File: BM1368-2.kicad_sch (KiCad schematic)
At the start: 39 parts, among them U12 BM1368_mode1, U13 BM1368_mode1

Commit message: DRC Check
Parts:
- removed R51: 10k, Resistor_SMD:R_0805_2012Metric, symbol Device:R
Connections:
- net U13-VDD1_1: now reaches C146.2, C147.1, U13.28 (VDD1_1)
- net U13-VDD2_1: now reaches C145.2, C146.1, U13.29 (VDD2_1)
- net U13-VDD3_1: now reaches C144.2, C145.1, U13.30 (VDD3_1)
- net Net-(U11-VDD1_1) renamed U11-VDD1_1
- net Net-(U11-VDD2_1) renamed U11-VDD2_1
- net Net-(U11-VDD3_1) renamed U11-VDD3_1
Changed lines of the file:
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@@
 	)
 	(junction
+		(at 234.95 45.72)
+		(diameter 0)
+		(color 0 0 0 0)
+	)
+	(junction
+		(at 257.81 50.8)
+		(diameter 0)
+		(color 0 0 0 0)
+	)
+	(junction
 		(at 184.15 36.83)
 		(diameter 0)
@@
 	)
 	(junction
+		(at 78.74 45.72)
+		(diameter 0)
+		(color 0 0 0 0)
+	)
+	(junction
+		(at 54.61 50.8)
+		(diameter 0)
+		(color 0 0 0 0)
+	)
+	(junction
 		(at 139.7 55.88)
 		(diameter 0)
@@
 	)
 	(junction
+		(at 67.31 48.26)
+		(diameter 0)
+		(color 0 0 0 0)
+	)
+	(junction
 		(at 234.95 53.34)
 		(diameter 0)
@@
 	)
 	(junction
-		(at 234.95 76.2)
+		(at 246.38 48.26)
 		(diameter 0)
 		(color 0 0 0 0)
 	)
 	(junction
-		(at 97.79 36.83)
+		(at 234.95 76.2)
 		(diameter 0)
 		(color 0 0 0 0)
 	)
 	(junction
-		(at 254 55.88)
+		(at 97.79 36.83)
 		(diameter 0)
 		(color 0 0 0 0)
@@
 	(wire
 		(pts
+			(xy 257.81 50.8) (xy 275.59 50.8)
+		)
+		(stroke
+			(width 0)
+			(type default)
+		)
+	)
+	(wire
+		(pts
 			(xy 181.61 71.12) (xy 196.85 71.12)
 		)
@@
 	(wire
 		(pts
-			(xy 254 55.88) (xy 254 77.47)
-		)
-		(stroke
-			(width 0)
-			(type default)
-		)
-	)
-	(wire
-		(pts
 			(xy 97.79 34.29) (xy 97.79 36.83)
 		)
@@
 	(wire
 		(pts
-			(xy 254 55.88) (xy 274.32 55.88)
+			(xy 232.41 55.88) (xy 274.32 55.88)
 		)
 		(stroke
@@
 	(wire
 		(pts
+			(xy 30.48 45.72) (xy 78.74 45.72)
+		)
+		(stroke
+			(width 0)
+			(type default)
+		)
+	)
+	(wire
+		(pts
 			(xy 214.63 36.83) (xy 222.25 36.83)
 		)
@@
 	(wire
 		(pts
-			(xy 214.63 86.36) (xy 214.63 91.44)
+			(xy 246.38 48.26) (xy 275.59 48.26)
 		)
 		(stroke
@@
 	(wire
 		(pts
-			(xy 195.58 36.83) (xy 195.58 45.72)
+			(xy 214.63 86.36) (xy 214.63 91.44)
 		)
 		(stroke
@@
 	(wire
 		(pts
-			(xy 254 85.09) (xy 254 87.63)
+			(xy 195.58 36.83) (xy 195.58 45.72)
 		)
 		(stroke
@@
 	(wire
 		(pts
+			(xy 234.95 45.72) (xy 275.59 45.72)
+		)
+		(stroke
+			(width 0)
+			(type default)
+		)
+	)
+	(wire
+		(pts
 			(xy 73.66 146.05) (xy 73.66 147.32)
 		)
@@
 	(wire
 		(pts
-			(xy 257.81 50.8) (xy 257.81 36.83)
+			(xy 30.48 48.26) (xy 67.31 48.26)
 		)
 		(stroke
@@
 	(wire
 		(pts
-			(xy 232.41 55.88) (xy 254 55.88)
+			(xy 257.81 50.8) (xy 257.81 36.83)
 		)
 		(stroke
@@
 	(wire
 		(pts
+			(xy 30.48 50.8) (xy 54.61 50.8)
+		)
+		(stroke
+			(width 0)
+			(type default)
+		)
+	)
+	(wire
+		(pts
 			(xy 78.74 36.83) (xy 78.74 45.72)
 		)
@@
 		)
 	)
-	(label "Net-(U11-VDD3_1)"
-		(at 78.74 36.83 90)
+	(hierarchical_label "NRSTO"
+		(shape output)
+		(at 274.32 55.88 0)
 		(fields_autoplaced yes)
 		(effects
@@
 				(size 1.27 1.27)
 			)
-			(justify left bottom)
+			(justify left)
 		)
 	)
-	(label "Net-(U11-VDD1_1)"
-		(at 54.61 50.8 0)
+	(hierarchical_label "RI"
+		(shape input)
+		(at 270.51 60.96 0)
 		(fields_autoplaced yes)
 		(effects
@@
 				(size 1.27 1.27)
 			)
-			(justify left bottom)
+			(justify left)
 		)
 	)
-	(label "Net-(U11-VDD2_1)"
-		(at 67.31 36.83 90)
+	(hierarchical_label "U11-VDD3_1"
+		(shape input)
+		(at 30.48 45.72 180)
 		(fields_autoplaced yes)
 		(effects
@@
 				(size 1.27 1.27)
 			)
-			(justify left bottom)
+			(justify right)
 		)
 	)
-	(hierarchical_label "NRSTO"
+	(hierarchical_label "BI"
+		(shape input)
+		(at 62.23 66.04 180)
+		(fields_autoplaced yes)
+		(effects
+			(font
+				(size 1.27 1.27)
+			)
+			(justify right)
+		)
+	)
+	(hierarchical_label "U13-VDD2_1"
 		(shape output)
-		(at 274.32 55.88 0)
+		(at 275.59 48.26 0)
 		(fields_autoplaced yes)
 		(effects
@@
 		)
 	)
-	(hierarchical_label "RI"
-		(shape input)
-		(at 270.51 60.96 0)
+	(hierarchical_label "CLKO"
+		(shape output)
+		(at 269.24 63.5 0)
 		(fields_autoplaced yes)
 		(effects
@@
 		)
 	)
-	(hierarchical_label "BI"
+	(hierarchical_label "CI"
 		(shape input)
-		(at 62.23 66.04 180)
+		(at 60.96 58.42 180)
 		(fields_autoplaced yes)
 		(effects
@@
 		)
 	)
-	(hierarchical_label "CLKO"
-		(shape output)
-		(at 269.24 63.5 0)
+	(hierarchical_label "U11-VDD1_1"
+		(shape input)
+		(at 30.48 50.8 180)
 		(fields_autoplaced yes)
 		(effects
@@
 				(size 1.27 1.27)
 			)
-			(justify left)
+			(justify right)
 		)
 	)
-	(hierarchical_label "CI"
+	(hierarchical_label "U11-VDD2_1"
 		(shape input)
-		(at 60.96 58.42 180)
+		(at 30.48 48.26 180)
 		(fields_autoplaced yes)
 		(effects
@@
 		)
 	)
+	(hierarchical_label "U13-VDD1_1"
+		(shape output)
+		(at 275.59 50.8 0)
+		(fields_autoplaced yes)
+		(effects
+			(font
+				(size 1.27 1.27)
+			)
+			(justify left)
+		)
+	)
 	(hierarchical_label "CLKI"
 		(shape input)
@@
 		)
 	)
+	(hierarchical_label "U13-VDD3_1"
+		(shape output)
+		(at 275.59 45.72 0)
+		(fields_autoplaced yes)
+		(effects
+			(font
+				(size 1.27 1.27)
+			)
+			(justify left)
+		)
+	)
 	(symbol
 		(lib_id "power:+1V2")
@@
 	)
 	(symbol
-		(lib_id "Device:R")
-		(at 254 81.28 0)
-		(unit 1)
-		(exclude_from_sim no)
-		(in_bom yes)
-		(on_board yes)
-		(dnp no)
-		(property "Reference" "R51"
-			(at 251.714 80.772 90)
-			(effects
-				(font
-					(size 1.27 1.27)
-				)
-			)
-		)
-		(property "Value" "10k"
-			(at 255.905 80.645 90)
-			(effects
-				(font
-					(size 1.27 1.27)
-				)
-			)
-		)
-		(property "Footprint" "Resistor_SMD:R_0805_2012Metric"
-			(at 252.222 81.28 90)
-			(effects
-				(font
-					(size 1.27 1.27)
-				)
-				(hide yes)
-			)
-		)
-		(property "Datasheet" "~"
-			(at 254 81.28 0)
-			(effects
-				(font
-					(size 1.27 1.27)
-				)
-				(hide yes)
-			)
-		)
-		(property "Description" ""
-			(at 254 81.28 0)
-			(effects
-				(font
-					(size 1.27 1.27)
-				)
-				(hide yes)
-			)
-		)
-		(pin "1"
-		)
-		(pin "2"
-		)
-		(instances
-			(project "Nerd8"
-				(path "/e63e39d7-6ac0-4ffd-8aa3-1841a4541b55/4cf9c075-d009-4c35-9949-adda70ae20c7/e80b0a8e-8746-4c15-aedd-74be2900e512"
-					(reference "R51")
-					(unit 1)
-				)
-			)
-		)
-	)
-	(symbol
 		(lib_id "Device:C")
 		(at 60.96 36.83 90)
@@
 					(unit 1)
 				)
-			)
-		)
-	)
-	(symbol
-		(lib_id "power:+1V8")
-		(at 254 87.63 180)
-		(unit 1)
-		(exclude_from_sim no)
-		(in_bom yes)
-		(on_board yes)
-		(dnp no)
-		(property "Reference" "#PWR0365"
-			(at 254 83.82 0)
-			(effects
-				(font
-					(size 1.27 1.27)
-				)
-				(hide yes)
-			)
-		)
-		(property "Value" "GND"
-			(at 254 92.71 90)
-			(effects
-				(font
-					(size 1.27 1.27)
-				)
-			)
-		)
-		(property "Footprint" ""
-			(at 254 87.63 0)
-			(effects
-				(font
-					(size 1.27 1.27)
-				)
-				(hide yes)
-			)
-		)
-		(property "Datasheet" ""
-			(at 254 87.63 0)
-			(effects
-				(font
-					(size 1.27 1.27)
-				)
-				(hide yes)
-			)
-		)
-		(property "Description" ""
-			(at 254 87.63 0)
-			(effects
-				(font
-					(size 1.27 1.27)
-				)
-				(hide yes)
-			)
-		)
-		(pin "1"
-		)
-		(instances
-			(project "Nerd8"
-				(path "/e63e39d7-6ac0-4ffd-8aa3-1841a4541b55/4cf9c075-d009-4c35-9949-adda70ae20c7/e80b0a8e-8746-4c15-aedd-74be2900e512"
-					(reference "#PWR0365")
-					(unit 1)
-				)

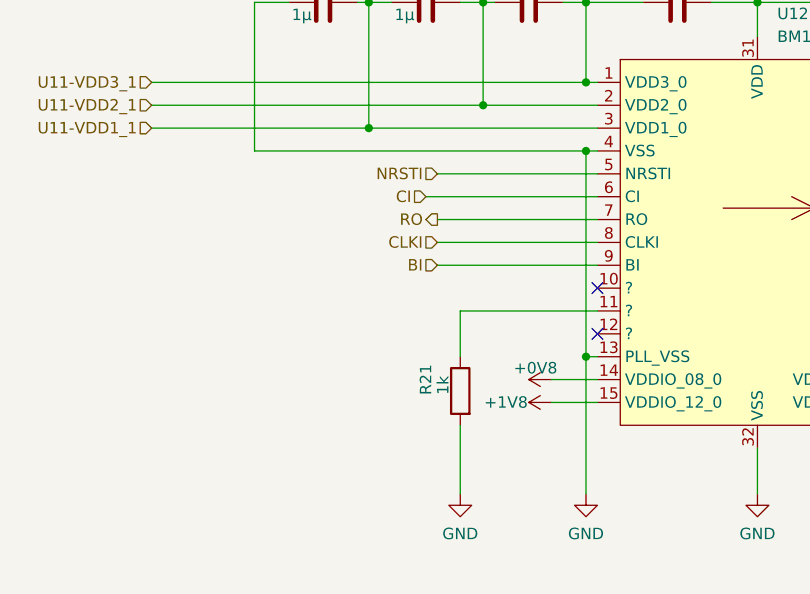
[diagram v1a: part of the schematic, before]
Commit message: References and Logos
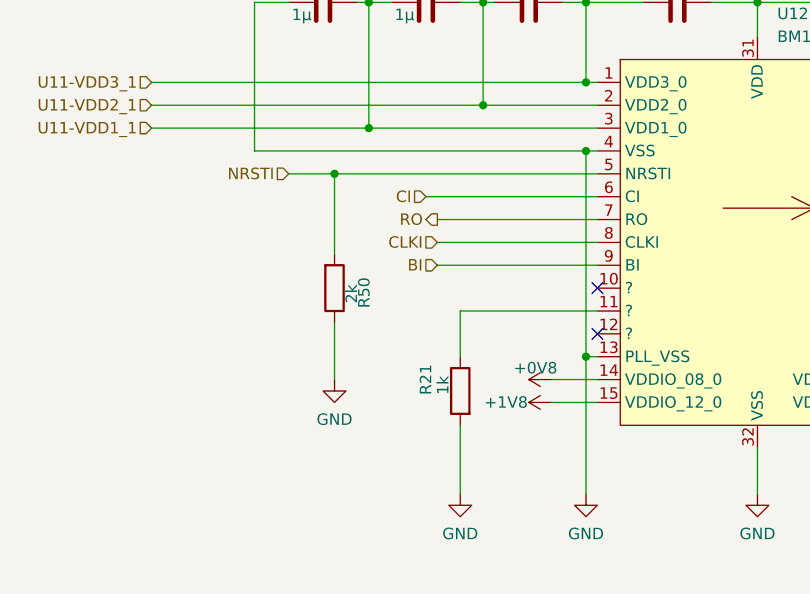
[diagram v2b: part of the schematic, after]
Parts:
- added R50: 2k, Resistor_SMD:R_0805_2012Metric, symbol Device:R
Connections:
- net GND: now also R50.1
- net NRSTI: now also R50.2
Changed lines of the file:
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@@
 	)
 	(junction
+		(at 50.8 55.88)
+		(diameter 0)
+		(color 0 0 0 0)
+	)
+	(junction
 		(at 78.74 45.72)
 		(diameter 0)
@@
 	(wire
 		(pts
+			(xy 50.8 72.39) (xy 50.8 78.74)
+		)
+		(stroke
+			(width 0)
+			(type default)
+		)
+	)
+	(wire
+		(pts
 			(xy 111.76 146.05) (xy 111.76 147.32)
 		)
@@
 	(wire
 		(pts
+			(xy 50.8 55.88) (xy 50.8 64.77)
+		)
+		(stroke
+			(width 0)
+			(type default)
+		)
+	)
+	(wire
+		(pts
 			(xy 31.75 146.05) (xy 31.75 147.32)
 		)
@@
 	(wire
 		(pts
+			(xy 50.8 55.88) (xy 80.01 55.88)
+		)
+		(stroke
+			(width 0)
+			(type default)
+		)
+	)
+	(wire
+		(pts
 			(xy 78.74 45.72) (xy 80.01 45.72)
 		)
@@
 	(wire
 		(pts
-			(xy 62.23 55.88) (xy 80.01 55.88)
+			(xy 45.72 55.88) (xy 50.8 55.88)
 		)
 		(stroke
@@
 	(hierarchical_label "NRSTI"
 		(shape input)
-		(at 62.23 55.88 180)
+		(at 45.72 55.88 180)
 		(fields_autoplaced yes)
 		(effects
@@
 	)
 	(symbol
+		(lib_id "Device:R")
+		(at 50.8 68.58 0)
+		(mirror x)
+		(unit 1)
+		(exclude_from_sim no)
+		(in_bom yes)
+		(on_board yes)
+		(dnp no)
+		(property "Reference" "R50"
+			(at 54.102 69.088 90)
+			(effects
+				(font
+					(size 1.27 1.27)
+				)
+			)
+		)
+		(property "Value" "2k"
+			(at 52.705 69.215 90)
+			(effects
+				(font
+					(size 1.27 1.27)
+				)
+			)
+		)
+		(property "Footprint" "Resistor_SMD:R_0805_2012Metric"
+			(at 49.022 68.58 90)
+			(effects
+				(font
+					(size 1.27 1.27)
+				)
+				(hide yes)
+			)
+		)
+		(property "Datasheet" "~"
+			(at 50.8 68.58 0)
+			(effects
+				(font
+					(size 1.27 1.27)
+				)
+				(hide yes)
+			)
+		)
+		(property "Description" ""
+			(at 50.8 68.58 0)
+			(effects
+				(font
+					(size 1.27 1.27)
+				)
+				(hide yes)
+			)
+		)
+		(pin "1"
+		)
+		(pin "2"
+		)
+		(instances
+			(project "Nerd8"
+				(path "/e63e39d7-6ac0-4ffd-8aa3-1841a4541b55/4cf9c075-d009-4c35-9949-adda70ae20c7/e80b0a8e-8746-4c15-aedd-74be2900e512"
+					(reference "R50")
+					(unit 1)
+				)
+			)
+		)
+	)
+	(symbol
 		(lib_id "Device:C")
 		(at 146.05 142.24 0)
@@
 					(unit 1)
 				)
+			)
+		)
+	)
+	(symbol
+		(lib_id "power:GND")
+		(at 50.8 78.74 0)
+		(mirror y)
+		(unit 1)
+		(exclude_from_sim no)
+		(in_bom yes)
+		(on_board yes)
+		(dnp no)
+		(fields_autoplaced yes)
+		(property "Reference" "#PWR0340"
+			(at 50.8 85.09 0)
+			(effects
+				(font
+					(size 1.27 1.27)
+				)
+				(hide yes)
+			)
+		)
+		(property "Value" "GND"
+			(at 50.8 83.185 0)
+			(effects
+				(font
+					(size 1.27 1.27)
+				)
+			)
+		)
+		(property "Footprint" ""
+			(at 50.8 78.74 0)
+			(effects
+				(font
+					(size 1.27 1.27)
+				)
+				(hide yes)
+			)
+		)
+		(property "Datasheet" ""
+			(at 50.8 78.74 0)
+			(effects
+				(font
+					(size 1.27 1.27)
+				)
+				(hide yes)
+			)
+		)
+		(property "Description" ""
+			(at 50.8 78.74 0)
+			(effects
+				(font
+					(size 1.27 1.27)
+				)
+				(hide yes)
+			)
+		)
+		(pin "1"
+		)
+		(instances
+			(project "Nerd8"
+				(path "/e63e39d7-6ac0-4ffd-8aa3-1841a4541b55/4cf9c075-d009-4c35-9949-adda70ae20c7/e80b0a8e-8746-4c15-aedd-74be2900e512"
+					(reference "#PWR0340")
+					(unit 1)
+				)
